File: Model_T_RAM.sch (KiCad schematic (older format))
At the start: 3 parts, among them J1 KC-85_RAM, U1 6264, U2 74HC86

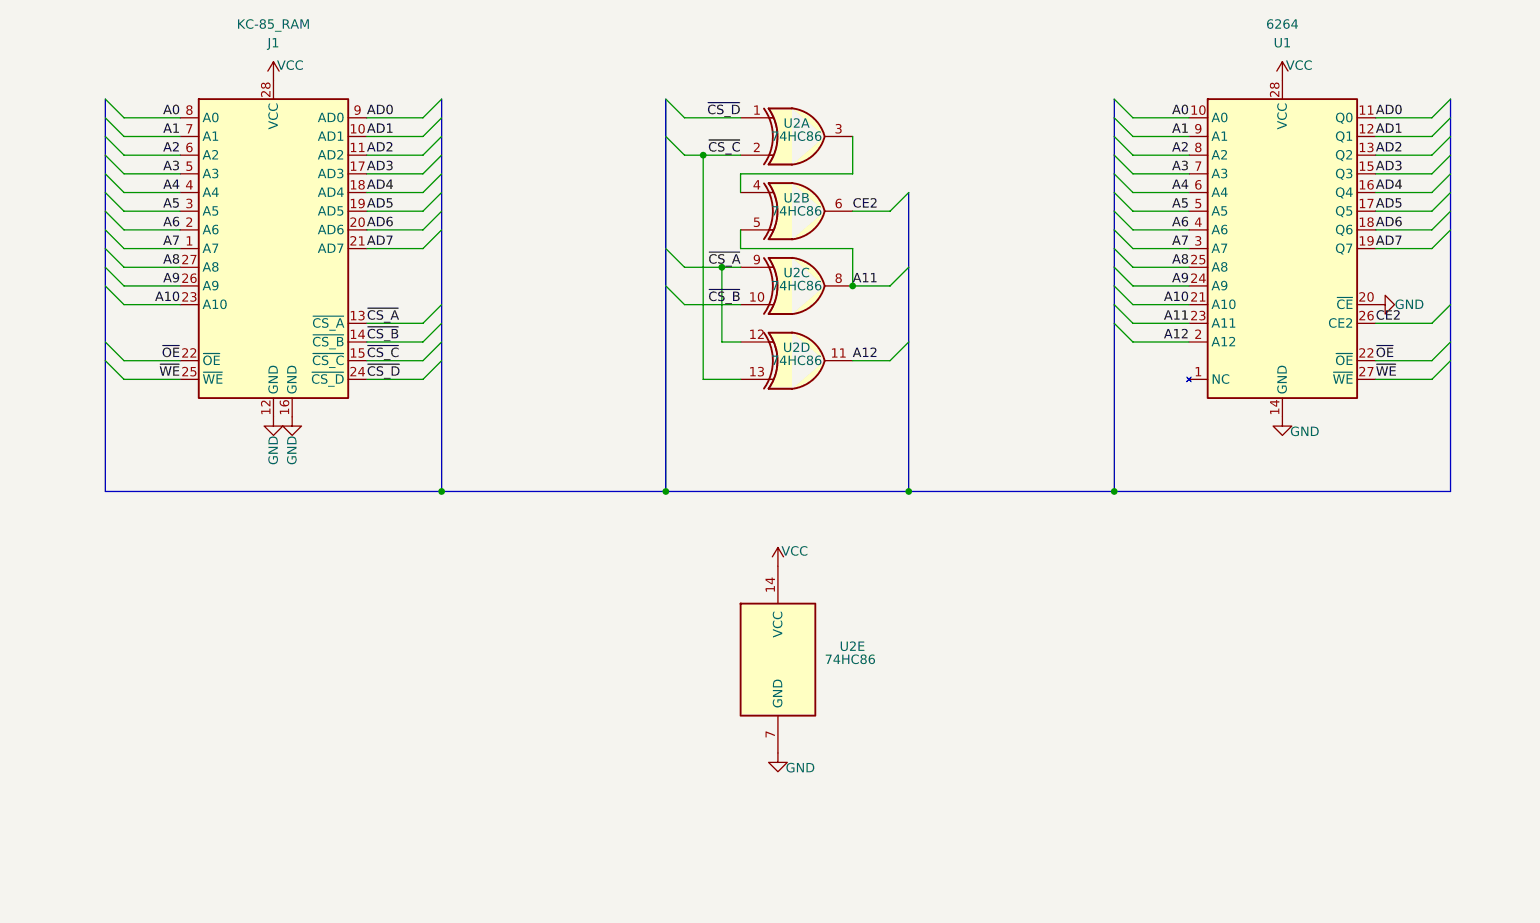
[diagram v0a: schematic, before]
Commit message: switch to 74HC08
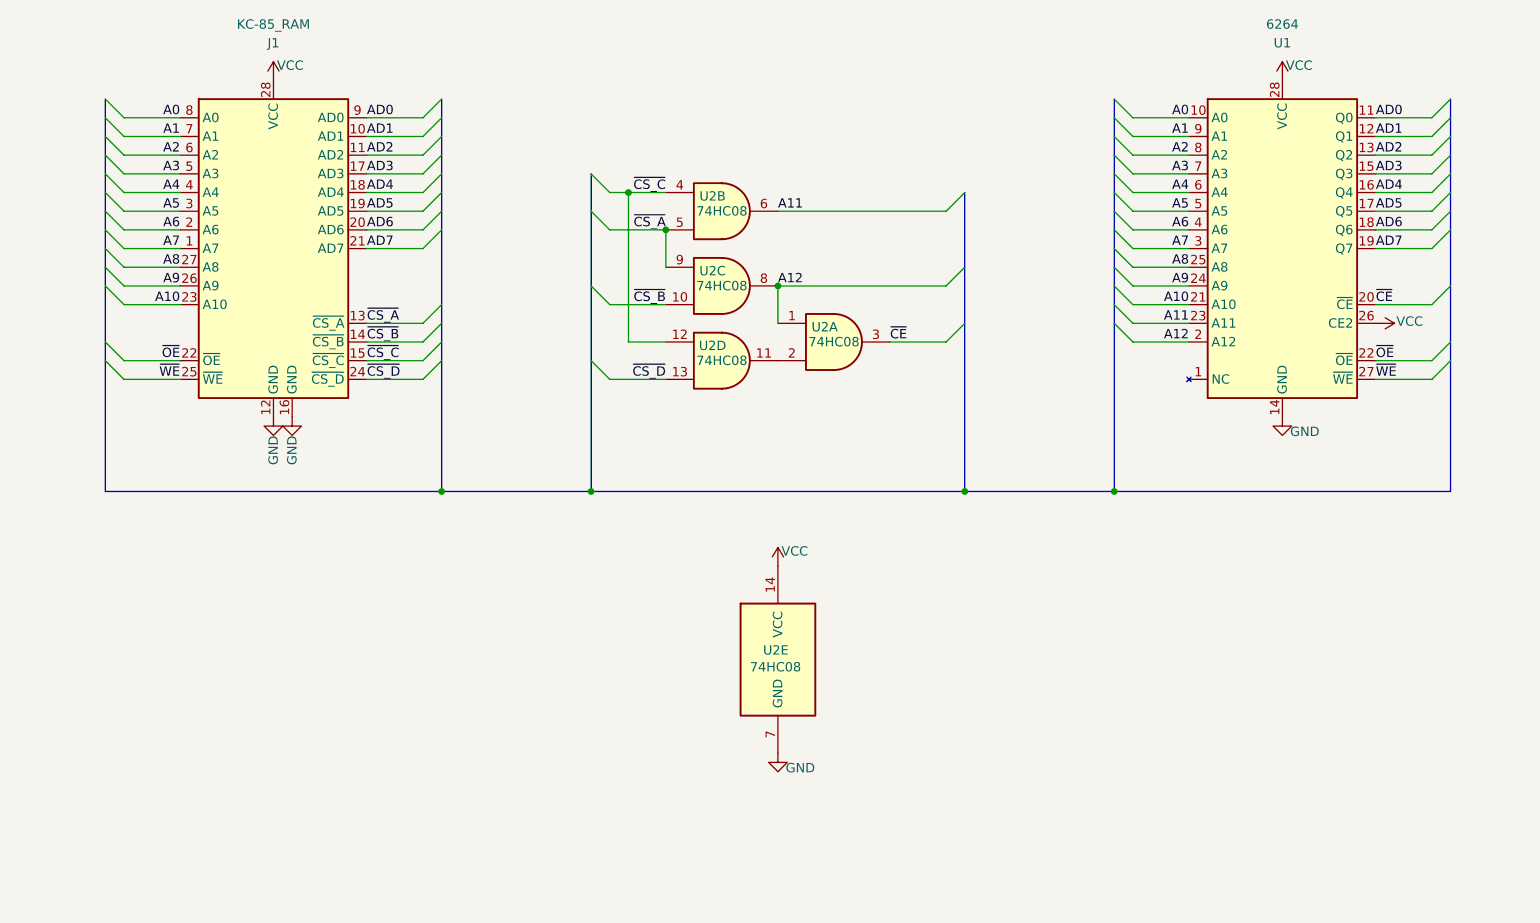
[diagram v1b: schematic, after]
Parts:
- removed U2: 74HC86, 000_LOCAL:SOIC-14_3.9x8.7mm_P1.27mm, symbol 000_LOCAL:74HC86
- added U2: 74HC08, 000_LOCAL:SOIC-14_3.9x8.7mm_P1.27mm, symbol 000_LOCAL:74HC08
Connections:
- net CE2 is gone; now on net VCC: U1.26 (CE2)
- net A11: now also U2.6
- net A12: now also U2.1, U2.8
- net GND: now also U2.7 (GND); no longer U1.20 (~CE)
- net VCC: now also U2.14 (VCC)
- net ~CS_A: now also U2.5, U2.9
- net ~CS_B: now also U2.10
- net ~CS_C: now also U2.12, U2.4
- net ~CS_D: now also U2.13
- new net: U2.11, U2.2
- new net ~CE: U1.20 (~CE), U2.3
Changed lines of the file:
@@
 Sheet 1 1
 Title "Model T RAM Module"
-Date "2021-04-13"
-Rev "001"
+Date "2021-04-20"
+Rev "003"
 Comp "b.kenyon.w@gmail.com"
 Comment1 ""
@@
 F 1 "6264" H 7900 4900 50  0000 C CNN
 F 2 "000_LOCAL:AS6C6264-55SCN" H 7900 3600 50  0001 C CNN
-F 3 "https://www.futurlec.com/Datasheet/Memory/62256.pdf" H 7900 3600 50  0001 C CNN
+F 3 "" H 7900 3600 50  0001 C CNN
 	1    7900 3700
 	1    0    0    -1
@@
 	7100 4200 7400 4200
 Wire Wire Line
-	8400 4100 8700 4100
-Entry Wire Line
-	8700 4100 8800 4000
+	8400 4000 8700 4000
+Entry Wire Line
+	8700 4000 8800 3900
 Wire Wire Line
 	8400 4300 8700 4300
@@
 $EndComp
 $Comp
-L 000_LOCAL:74HC86 U2
-U 1 1 60785C24
-P 5300 3100
-F 0 "U2" H 5300 3170 50  0000 C CNN
-F 1 "74HC86" H 5300 3100 50  0000 C CNN
-F 2 "000_LOCAL:SOIC-14_3.9x8.7mm_P1.27mm" H 5300 3100 50  0001 C CNN
-F 3 "http://www.ti.com/lit/gpn/sn74HC86" H 5300 3100 50  0001 C CNN
-	1    5300 3100
-	1    0    0    -1
-$EndComp
-$Comp
-L 000_LOCAL:74HC86 U2
-U 5 1 60795F64
-P 5200 5900
-F 0 "U2" H 5530 5970 50  0000 L CNN
-F 1 "74HC86" H 5450 5900 50  0000 L CNN
-F 2 "000_LOCAL:SOIC-14_3.9x8.7mm_P1.27mm" H 5200 5900 50  0001 C CNN
-F 3 "http://www.ti.com/lit/gpn/sn74HC86" H 5200 5900 50  0001 C CNN
-	5    5200 5900
-	1    0    0    -1
-$EndComp
-$Comp
 L power:VCC #PWR0105
 U 1 1 607CD4E2
@@
 	1    0    0    -1
 $EndComp
-Entry Wire Line
-	4600 2900 4700 3000
-Wire Wire Line
-	5000 3000 4700 3000
 Text Label 3000 4400 0    50   ~ 0
 ~CS_D
-Text Label 5000 3000 2    50   ~ 0
-~CS_D
-Wire Wire Line
-	5000 3200 4800 3200
-Entry Wire Line
-	4600 3900 4700 4000
-Connection ~ 4600 5000
-Wire Bus Line
-	3400 5000 4600 5000
-Entry Wire Line
-	5800 3500 5900 3400
-Entry Wire Line
-	5800 4300 5900 4200
 Text Label 3000 4200 0    50   ~ 0
-~CS_B
-Text Label 5000 4000 2    50   ~ 0
 ~CS_B
 Text Label 3000 4300 0    50   ~ 0
 ~CS_C
-Text Label 5000 3200 2    50   ~ 0
-~CS_C
-Entry Wire Line
-	4600 3100 4700 3200
-Wire Wire Line
-	4800 3200 4700 3200
-Connection ~ 4800 3200
 Text Label 3000 4100 0    50   ~ 0
 ~CS_A
-Text Label 5600 3900 0    50   ~ 0
-A11
-Entry Wire Line
-	5800 3900 5900 3800
-Text Label 5600 4300 0    50   ~ 0
-A12
-Text Label 5600 3500 0    50   ~ 0
-CE2
-Text Label 8400 4100 0    50   ~ 0
-CE2
-$Comp
-L power:GND #PWR0107
-U 1 1 609A2377
-P 8400 4000
-F 0 "#PWR0107" H 8400 3750 50  0001 C CNN
-F 1 "GND" V 8400 3820 50  0000 C CNN
-F 2 "" H 8400 4000 50  0001 C CNN
-F 3 "" H 8400 4000 50  0001 C CNN
-	1    8400 4000
-	0    -1   -1   0
-$EndComp
-$Comp
-L 000_LOCAL:74HC86 U2
-U 2 1 607885D1
-P 5300 3500
-F 0 "U2" H 5300 3570 50  0000 C CNN
-F 1 "74HC86" H 5300 3500 50  0000 C CNN
-F 2 "000_LOCAL:SOIC-14_3.9x8.7mm_P1.27mm" H 5300 3500 50  0001 C CNN
-F 3 "http://www.ti.com/lit/gpn/sn74HC86" H 5300 3500 50  0001 C CNN
-	2    5300 3500
-	1    0    0    -1
-$EndComp
-Wire Wire Line
-	5000 4000 4700 4000
-$Comp
-L 000_LOCAL:74HC86 U2
-U 3 1 6078B6F7
-P 5300 3900
-F 0 "U2" H 5300 3970 50  0000 C CNN
-F 1 "74HC86" H 5300 3900 50  0000 C CNN
-F 2 "000_LOCAL:SOIC-14_3.9x8.7mm_P1.27mm" H 5300 3900 50  0001 C CNN
-F 3 "http://www.ti.com/lit/gpn/sn74HC86" H 5300 3900 50  0001 C CNN
-	3    5300 3900
-	1    0    0    -1
-$EndComp
-$Comp
-L 000_LOCAL:74HC86 U2
-U 4 1 607904BD
-P 5300 4300
-F 0 "U2" H 5300 4370 50  0000 C CNN
-F 1 "74HC86" H 5300 4300 50  0000 C CNN
-F 2 "000_LOCAL:SOIC-14_3.9x8.7mm_P1.27mm" H 5300 4300 50  0001 C CNN
-F 3 "http://www.ti.com/lit/gpn/sn74HC86" H 5300 4300 50  0001 C CNN
-	4    5300 4300
-	1    0    0    -1
-$EndComp
-Wire Wire Line
-	5000 4200 4900 4200
-Wire Wire Line
-	4900 4200 4900 3800
-Wire Wire Line
-	4900 3800 5000 3800
-Wire Wire Line
-	5000 4400 4800 4400
-Wire Wire Line
-	4800 3200 4800 4400
-Wire Wire Line
-	5000 3600 5000 3700
-Wire Wire Line
-	5000 3700 5600 3700
-Wire Wire Line
-	5600 3700 5600 3900
-Wire Wire Line
-	5000 3400 5000 3300
-Wire Wire Line
-	5000 3300 5600 3300
-Wire Wire Line
-	5600 3300 5600 3100
-Wire Bus Line
-	4600 5000 5900 5000
-Connection ~ 5900 5000
-Wire Bus Line
-	5900 5000 7000 5000
-Wire Wire Line
-	5600 3900 5800 3900
-Connection ~ 5600 3900
-Wire Wire Line
-	5600 4300 5800 4300
-Wire Wire Line
-	5600 3500 5800 3500
-Connection ~ 4900 3800
-Wire Wire Line
-	4700 3800 4900 3800
-Entry Wire Line
-	4600 3700 4700 3800
-Text Label 5000 3800 2    50   ~ 0
-~CS_A
+Text Label 8400 4000 0    50   ~ 0
+~CE
 Text Label 7400 4100 2    50   ~ 0
 A11
@@
 	7000 5000 8800 5000
 Wire Bus Line
-	5900 3400 5900 5000
-Wire Bus Line
-	4600 2900 4600 5000
+	3400 5000 4200 5000
+$Comp
+L 000_LOCAL:74HC08 U2
+U 5 1 608031FE
+P 5200 5900
+F 0 "U2" H 5120 5950 50  0000 L CNN
+F 1 "74HC08" H 5050 5860 50  0000 L CNN
+F 2 "000_LOCAL:SOIC-14_3.9x8.7mm_P1.27mm" H 5200 5900 50  0001 C CNN
+F 3 "http://www.ti.com/lit/gpn/sn74LS08" H 5200 5900 50  0001 C CNN
+	5    5200 5900
+	1    0    0    -1
+$EndComp
+$Comp
+L 000_LOCAL:74HC08 U2
+U 1 1 608063D1
+P 5500 4200
+F 0 "U2" H 5450 4280 50  0000 C CNN
+F 1 "74HC08" H 5500 4200 50  0000 C CNN
+F 2 "000_LOCAL:SOIC-14_3.9x8.7mm_P1.27mm" H 5500 4200 50  0001 C CNN
+F 3 "http://www.ti.com/lit/gpn/sn74LS08" H 5500 4200 50  0001 C CNN
+	1    5500 4200
+	1    0    0    -1
+$EndComp
+$Comp
+L 000_LOCAL:74HC08 U2
+U 2 1 60815F59
+P 4900 3500
+F 0 "U2" H 4850 3580 50  0000 C CNN
+F 1 "74HC08" H 4900 3500 50  0000 C CNN
+F 2 "000_LOCAL:SOIC-14_3.9x8.7mm_P1.27mm" H 4900 3500 50  0001 C CNN
+F 3 "http://www.ti.com/lit/gpn/sn74LS08" H 4900 3500 50  0001 C CNN
+	2    4900 3500
+	1    0    0    -1
+$EndComp
+$Comp
+L 000_LOCAL:74HC08 U2
+U 3 1 6081B7BF
+P 4900 3900
+F 0 "U2" H 4850 3980 50  0000 C CNN
+F 1 "74HC08" H 4900 3900 50  0000 C CNN
+F 2 "000_LOCAL:SOIC-14_3.9x8.7mm_P1.27mm" H 4900 3900 50  0001 C CNN
+F 3 "http://www.ti.com/lit/gpn/sn74LS08" H 4900 3900 50  0001 C CNN
+	3    4900 3900
+	1    0    0    -1
+$EndComp
+$Comp
+L 000_LOCAL:74HC08 U2
+U 4 1 6081F8E2
+P 4900 4300
+F 0 "U2" H 4850 4380 50  0000 C CNN
+F 1 "74HC08" H 4900 4300 50  0000 C CNN
+F 2 "000_LOCAL:SOIC-14_3.9x8.7mm_P1.27mm" H 4900 4300 50  0001 C CNN
+F 3 "http://www.ti.com/lit/gpn/sn74LS08" H 4900 4300 50  0001 C CNN
+	4    4900 4300
+	1    0    0    -1
+$EndComp
+Entry Wire Line
+	4200 4300 4300 4400
+Wire Wire Line
+	4300 4400 4600 4400
+Entry Wire Line
+	4200 3300 4300 3400
+Wire Wire Line
+	4300 3400 4400 3400
+Text Label 4600 4400 2    50   ~ 0
+~CS_D
+Entry Wire Line
+	4200 3500 4300 3600
+Wire Wire Line
+	4300 3600 4600 3600
+Entry Wire Line
+	4200 3900 4300 4000
+Wire Wire Line
+	4300 4000 4600 4000
+Text Label 4600 3600 2    50   ~ 0
+~CS_A
+Text Label 4600 4000 2    50   ~ 0
+~CS_B
+Text Label 4600 3400 2    50   ~ 0
+~CS_C
+Wire Wire Line
+	5800 4200 6100 4200
+Entry Wire Line
+	6100 4200 6200 4100
+Text Label 5800 4200 0    50   ~ 0
+~CE
+Wire Wire Line
+	5200 3500 6100 3500
+Entry Wire Line
+	6100 3500 6200 3400
+Text Label 5200 3500 0    50   ~ 0
+A11
+$Comp
+L power:VCC #PWR0107
+U 1 1 608C614D
+P 8400 4100
+F 0 "#PWR0107" H 8400 3950 50  0001 C CNN
+F 1 "VCC" V 8390 4210 50  0000 L CNN
+F 2 "" H 8400 4100 50  0001 C CNN
+F 3 "" H 8400 4100 50  0001 C CNN
+	1    8400 4100
+	0    1    1    0
+$EndComp
+Wire Wire Line
+	5200 3900 6100 3900
+Entry Wire Line
+	6100 3900 6200 3800
+Text Label 5200 3900 0    50   ~ 0
+A12
+Wire Wire Line
+	4400 3400 4600 3400
+Wire Wire Line
+	4400 4200 4600 4200
+Connection ~ 4400 3400
+Wire Wire Line
+	4400 3400 4400 4200
+Connection ~ 4600 3600
+Wire Wire Line
+	4600 3600 4600 3800
+Connection ~ 5200 3900
+Wire Wire Line
+	5200 3900 5200 4100
+Connection ~ 4200 5000
+Connection ~ 6200 5000
+Wire Bus Line
+	4200 5000 6200 5000
+Wire Bus Line
+	6200 5000 7000 5000
+Wire Bus Line
+	6200 3400 6200 5000
+Wire Bus Line
+	4200 3300 4200 5000
 Wire Bus Line
 	8800 2900 8800 5000

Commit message: remove 74HC86 b version
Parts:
- U2: footprint 000_LOCAL:SOIC-14_3.9x8.7mm_P1.27mm -> 000_LOCAL:SOIC-14_4x9
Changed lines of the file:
@@
 F 0 "U2" H 5120 5950 50  0000 L CNN
 F 1 "74HC08" H 5050 5860 50  0000 L CNN
-F 2 "000_LOCAL:SOIC-14_3.9x8.7mm_P1.27mm" H 5200 5900 50  0001 C CNN
+F 2 "000_LOCAL:SOIC-14_4x9" H 5200 5900 50  0001 C CNN
 F 3 "http://www.ti.com/lit/gpn/sn74LS08" H 5200 5900 50  0001 C CNN
 	5    5200 5900
@@
 F 0 "U2" H 5450 4280 50  0000 C CNN
 F 1 "74HC08" H 5500 4200 50  0000 C CNN
-F 2 "000_LOCAL:SOIC-14_3.9x8.7mm_P1.27mm" H 5500 4200 50  0001 C CNN
+F 2 "000_LOCAL:SOIC-14_4x9" H 5500 4200 50  0001 C CNN
 F 3 "http://www.ti.com/lit/gpn/sn74LS08" H 5500 4200 50  0001 C CNN
 	1    5500 4200
@@
 F 0 "U2" H 4850 3580 50  0000 C CNN
 F 1 "74HC08" H 4900 3500 50  0000 C CNN
-F 2 "000_LOCAL:SOIC-14_3.9x8.7mm_P1.27mm" H 4900 3500 50  0001 C CNN
+F 2 "000_LOCAL:SOIC-14_4x9" H 4900 3500 50  0001 C CNN
 F 3 "http://www.ti.com/lit/gpn/sn74LS08" H 4900 3500 50  0001 C CNN
 	2    4900 3500
@@
 F 0 "U2" H 4850 3980 50  0000 C CNN
 F 1 "74HC08" H 4900 3900 50  0000 C CNN
-F 2 "000_LOCAL:SOIC-14_3.9x8.7mm_P1.27mm" H 4900 3900 50  0001 C CNN
+F 2 "000_LOCAL:SOIC-14_4x9" H 4900 3900 50  0001 C CNN
 F 3 "http://www.ti.com/lit/gpn/sn74LS08" H 4900 3900 50  0001 C CNN
 	3    4900 3900
@@
 F 0 "U2" H 4850 4380 50  0000 C CNN
 F 1 "74HC08" H 4900 4300 50  0000 C CNN
-F 2 "000_LOCAL:SOIC-14_3.9x8.7mm_P1.27mm" H 4900 4300 50  0001 C CNN
+F 2 "000_LOCAL:SOIC-14_4x9" H 4900 4300 50  0001 C CNN
 F 3 "http://www.ti.com/lit/gpn/sn74LS08" H 4900 4300 50  0001 C CNN
 	4    4900 4300

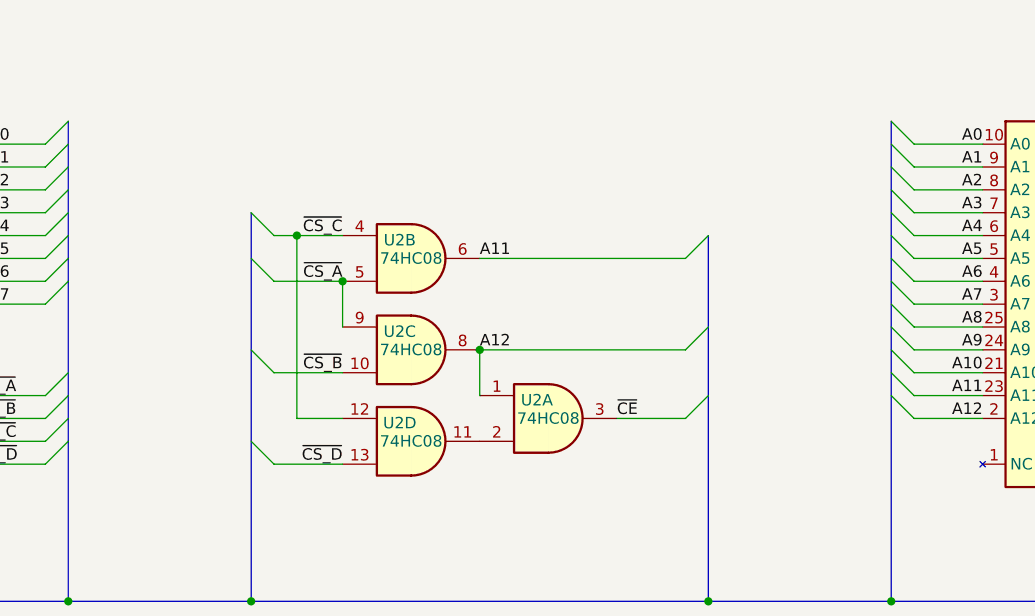
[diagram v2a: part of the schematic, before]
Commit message: prettify schematic, note power problem, mothball
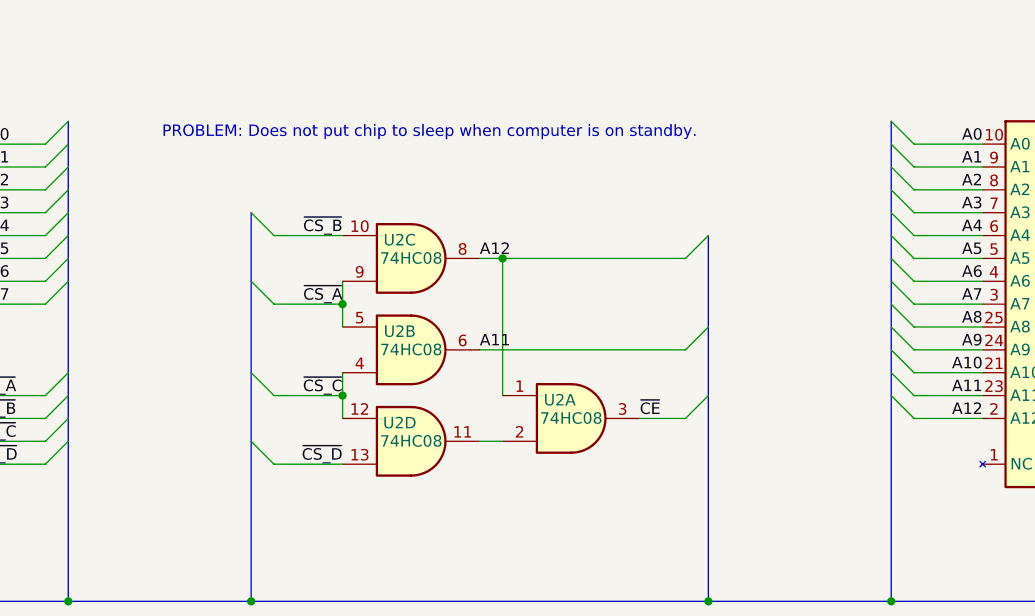
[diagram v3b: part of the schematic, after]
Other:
- note added: "PROBLEM: Does not put chip to sleep when computer is on standby."
- moved on the sheet: U2A, U2B, U2C
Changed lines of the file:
@@
 Sheet 1 1
 Title "Model T RAM Module"
-Date "2021-04-20"
-Rev "003"
+Date "2021-07-05"
+Rev "004"
 Comp "b.kenyon.w@gmail.com"
 Comment1 ""
@@
 L 000_LOCAL:74HC08 U2
 U 1 1 608063D1
-P 5500 4200
-F 0 "U2" H 5450 4280 50  0000 C CNN
-F 1 "74HC08" H 5500 4200 50  0000 C CNN
-F 2 "000_LOCAL:SOIC-14_4x9" H 5500 4200 50  0001 C CNN
-F 3 "http://www.ti.com/lit/gpn/sn74LS08" H 5500 4200 50  0001 C CNN
-	1    5500 4200
+P 5600 4200
+F 0 "U2" H 5550 4280 50  0000 C CNN
+F 1 "74HC08" H 5600 4200 50  0000 C CNN
+F 2 "000_LOCAL:SOIC-14_4x9" H 5600 4200 50  0001 C CNN
+F 3 "http://www.ti.com/lit/gpn/sn74LS08" H 5600 4200 50  0001 C CNN
+	1    5600 4200
 	1    0    0    -1
 $EndComp
@@
 L 000_LOCAL:74HC08 U2
 U 2 1 60815F59
+P 4900 3900
+F 0 "U2" H 4850 3820 50  0000 C CNN
+F 1 "74HC08" H 4900 3900 50  0000 C CNN
+F 2 "000_LOCAL:SOIC-14_4x9" H 4900 3900 50  0001 C CNN
+F 3 "http://www.ti.com/lit/gpn/sn74LS08" H 4900 3900 50  0001 C CNN
+	2    4900 3900
+	1    0    0    1
+$EndComp
+$Comp
+L 000_LOCAL:74HC08 U2
+U 3 1 6081B7BF
 P 4900 3500
-F 0 "U2" H 4850 3580 50  0000 C CNN
+F 0 "U2" H 4850 3420 50  0000 C CNN
 F 1 "74HC08" H 4900 3500 50  0000 C CNN
 F 2 "000_LOCAL:SOIC-14_4x9" H 4900 3500 50  0001 C CNN
 F 3 "http://www.ti.com/lit/gpn/sn74LS08" H 4900 3500 50  0001 C CNN
-	2    4900 3500
-	1    0    0    -1
-$EndComp
-$Comp
-L 000_LOCAL:74HC08 U2
-U 3 1 6081B7BF
-P 4900 3900
-F 0 "U2" H 4850 3980 50  0000 C CNN
-F 1 "74HC08" H 4900 3900 50  0000 C CNN
-F 2 "000_LOCAL:SOIC-14_4x9" H 4900 3900 50  0001 C CNN
-F 3 "http://www.ti.com/lit/gpn/sn74LS08" H 4900 3900 50  0001 C CNN
-	3    4900 3900
-	1    0    0    -1
+	3    4900 3500
+	1    0    0    1
 $EndComp
 $Comp
@@
 Entry Wire Line
 	4200 3300 4300 3400
-Wire Wire Line
-	4300 3400 4400 3400
 Text Label 4600 4400 2    50   ~ 0
 ~CS_D
 Entry Wire Line
-	4200 3500 4300 3600
-Wire Wire Line
-	4300 3600 4600 3600
-Entry Wire Line
-	4200 3900 4300 4000
-Wire Wire Line
-	4300 4000 4600 4000
-Text Label 4600 3600 2    50   ~ 0
-~CS_A
-Text Label 4600 4000 2    50   ~ 0
+	4200 3600 4300 3700
+Entry Wire Line
+	4200 4000 4300 4100
+Text Label 4600 3400 2    50   ~ 0
 ~CS_B
-Text Label 4600 3400 2    50   ~ 0
-~CS_C
-Wire Wire Line
-	5800 4200 6100 4200
 Entry Wire Line
 	6100 4200 6200 4100
-Text Label 5800 4200 0    50   ~ 0
+Text Label 5900 4200 0    50   ~ 0
 ~CE
-Wire Wire Line
-	5200 3500 6100 3500
 Entry Wire Line
 	6100 3500 6200 3400
-Text Label 5200 3500 0    50   ~ 0
+Text Label 5200 3900 0    50   ~ 0
 A11
 $Comp
@@
 	0    1    1    0
 $EndComp
-Wire Wire Line
-	5200 3900 6100 3900
 Entry Wire Line
 	6100 3900 6200 3800
-Text Label 5200 3900 0    50   ~ 0
+Text Label 5200 3500 0    50   ~ 0
 A12
-Wire Wire Line
-	4400 3400 4600 3400
-Wire Wire Line
-	4400 4200 4600 4200
-Connection ~ 4400 3400
-Wire Wire Line
-	4400 3400 4400 4200
-Connection ~ 4600 3600
-Wire Wire Line
-	4600 3600 4600 3800
-Connection ~ 5200 3900
-Wire Wire Line
-	5200 3900 5200 4100
 Connection ~ 4200 5000
 Connection ~ 6200 5000
@@
 Wire Bus Line
 	6200 5000 7000 5000
+Text Label 4600 3700 2    50   ~ 0
+~CS_A
+Text Label 4600 4100 2    50   ~ 0
+~CS_C
+Wire Wire Line
+	4600 4200 4600 4100
+Wire Wire Line
+	4600 4100 4300 4100
+Connection ~ 4600 4100
+Wire Wire Line
+	4600 4100 4600 4000
+Wire Wire Line
+	4600 3800 4600 3700
+Wire Wire Line
+	4600 3700 4300 3700
+Connection ~ 4600 3700
+Wire Wire Line
+	4600 3700 4600 3600
+Wire Wire Line
+	4600 3400 4300 3400
+Wire Wire Line
+	5200 3900 6100 3900
+Wire Wire Line
+	5200 4300 5300 4300
+Wire Wire Line
+	5200 3500 5300 3500
+Wire Wire Line
+	5300 4100 5300 3500
+Connection ~ 5300 3500
+Wire Wire Line
+	5300 3500 6100 3500
+Wire Wire Line
+	6100 4200 5900 4200
 Wire Bus Line
 	6200 3400 6200 5000
@@
 Wire Bus Line
 	7000 2900 7000 5000
+Text Notes 3810 2980 0    50   ~ 0
+PROBLEM: Does not put chip to sleep when computer is on standby.
 $EndSCHEMATC

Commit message: note RAM_RST
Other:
- note added: "PROBLEM: Does not put chip to sleep when machine is on standby."
- note added: "RAM_RST"
- note added: "~OE~ is RAM_RST, is high while machine is on standby"
- note removed: "PROBLEM: Does not put chip to sleep when computer is on standby."
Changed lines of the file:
@@
 Wire Wire Line
 	6100 4200 5900 4200
+Text Notes 3880 2980 0    50   ~ 0
+PROBLEM: Does not put chip to sleep when machine is on standby.
 Wire Bus Line
 	6200 3400 6200 5000
@@
 Wire Bus Line
 	7000 2900 7000 5000
-Text Notes 3810 2980 0    50   ~ 0
-PROBLEM: Does not put chip to sleep when computer is on standby.
+Text Notes 1500 4300 2    50   ~ 0
+RAM_RST
+Text Notes 1500 5320 0    50   ~ 0
+~OE~ is RAM_RST, is high while machine is on standby
 $EndSCHEMATC
